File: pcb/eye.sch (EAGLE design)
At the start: 89 parts, among them J2 JST-ZH-5SMD-RA, U1 WS2812, U10 WS2812, U11 WS2812, U12 WS2812, U13 WS2812, U14 WS2812, U15 WS2812, U16 WS2812, U17 WS2812, U18 WS2812, U19 WS2812, U2 WS2812, U20 WS2812, U21 WS2812, U22 WS2812, U23 WS2812, U24 WS2812, U25 WS2812, U26 WS2812, U27 WS2812, U28 WS2812, U29 WS2812, U3 WS2812, U30 WS2812, U31 WS2812, U32 WS2812, U33 WS2812, U34 WS2812, U35 WS2812, U36 WS2812, U37 WS2812, U38 WS2812, U39 WS2812, U4 WS2812, U40 WS2812, U41 WS2812, U42 WS2812, U43 WS2812, U44 WS2812, U45 WS2812, U46 WS2812, U47 WS2812, U48 WS2812, U49 WS2812, U5 WS2812, U50 WS2812, U51 WS2812, U52 WS2812, U53 WS2812, U54 WS2812, U55 WS2812, U56 WS2812, U57 WS2812, U58 WS2812, U59 WS2812, U6 WS2812, U60 WS2812, U61 32U4, U7 WS2812, U8 WS2812, U9 WS2812, X1 ECS-160-20-3X-TR

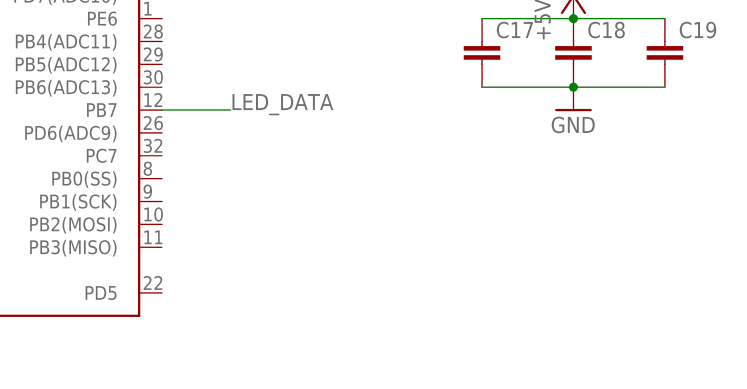
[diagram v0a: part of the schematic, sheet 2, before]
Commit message: add avr-isp header to glasses
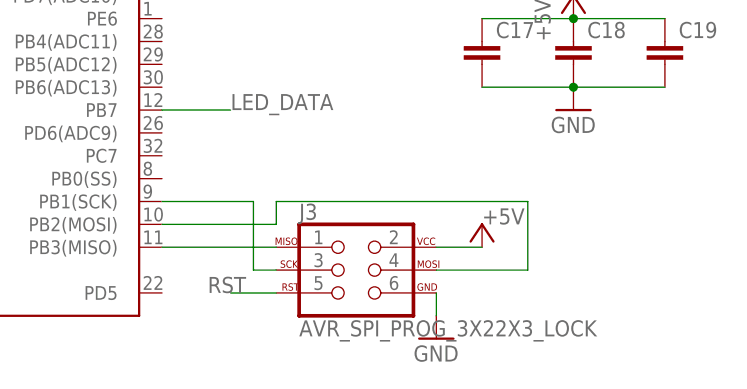
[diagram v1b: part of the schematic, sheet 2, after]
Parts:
- added J3: AVR_SPI_PROG_3X22X3_LOCK, SparkFun-Connectors:AVR_SPI_PROG_3X22X3_LOCK
- X1: device SparkFun-Clocks:CRYSTALSMD-3.2X1.5 -> SparkFun-Clocks:CRYSTALSMD-5X3.2-2PAD
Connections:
- new net N$65: J3.1, U61.PB3(MISO)
- new net N$66: J3.4, U61.PB2(MOSI)
- new net N$69: J3.3, U61.PB1(SCK)
- net +5V: now also J3.2
- net GND: now also J3.6
- net RST: now also J3.5
